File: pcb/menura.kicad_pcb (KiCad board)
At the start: 2 copper layers, 128.1 x 103.8 mm, 53 parts, among them SW1 SW_Push, SW10 SW_Push, SW11 SW_Push, SW12 SW_Push, SW13 SW_Push, SW14 SW_Push, SW15 SW_Push, SW16 SW_Push, SW17 SW_Push, SW18 SW_Push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

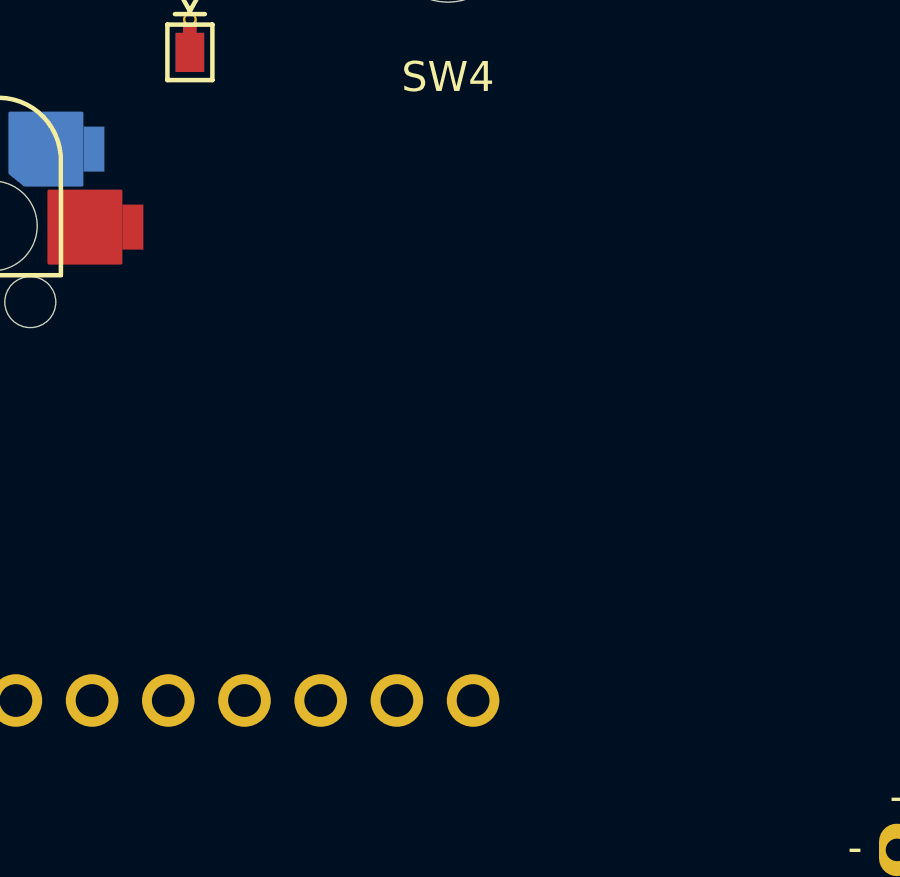
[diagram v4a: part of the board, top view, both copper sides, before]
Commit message: add vik throughole breakout
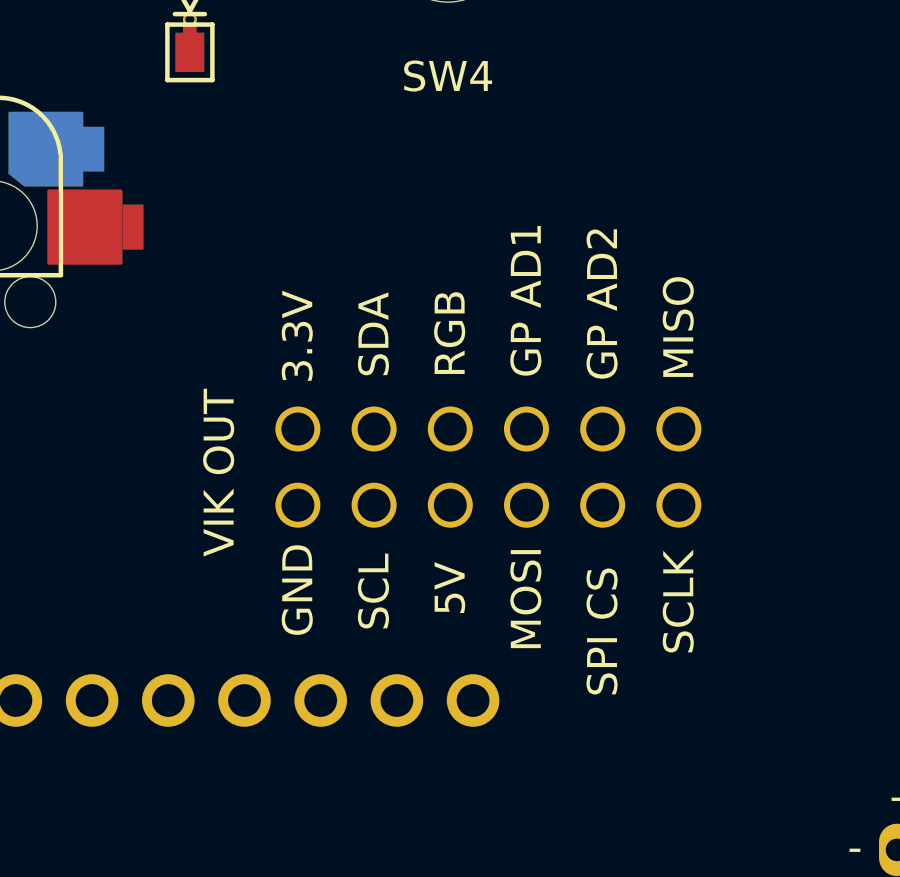
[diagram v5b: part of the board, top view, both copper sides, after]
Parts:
- added VIK2: ~, quappo:Connector_vik-keyboard-throughhole, F.Cu at (119.0, 105.5)

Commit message: tweak reset button placement
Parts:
- moved RSW1 19.8 mm to (128.6, 127.6), turned to 0 degrees
- moved PWR1 4.06 mm to (139.9, 128.6)
- moved JST1 4.00 mm to (139.9, 115.8)

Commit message: yaml comments
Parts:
- moved RSW1 2.83 mm to (130.1, 125.2), turned to -90 degrees
- moved MCU1 2.00 mm to (107.0, 120.5)
- moved PWR1 1.12 mm to (140.9, 128.1)
- moved JST1 1.00 mm to (140.9, 115.8)

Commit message: edge cut wip
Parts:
- moved JST1 2.22 mm to (140.9, 118.0)
- moved PWR1 1.84 mm to (140.9, 129.9)
- moved D18 0.95 mm to (157.0, 119.0)
- moved D21 0.95 mm to (167.1, 119.4)
- moved D22 0.95 mm to (186.9, 122.9)
- moved SW18 0.95 mm to (157.0, 110.8)
- moved SW20 0.95 mm to (199.3, 118.3)
- moved D19 0.95 mm to (177.1, 120.8)
- moved D20 0.95 mm to (196.5, 126.0)
- moved SW19 0.95 mm to (178.5, 112.7)
- moved SW21 0.95 mm to (167.8, 111.3)
- moved SW22 0.95 mm to (189.0, 115.0)
- moved VIK1 0.95 mm to (192.7, 101.4)
- moved RSW1 0.13 mm to (130.1, 125.3)
- moved MCU1 0.11 mm to (107.0, 120.6)
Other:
- board size 128.1 x 103.8 mm -> 123.3 x 97.2 mm
